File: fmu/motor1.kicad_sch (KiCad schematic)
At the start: 12 parts, among them J4 2213932-3, U4 MCF8316A1VRGFR

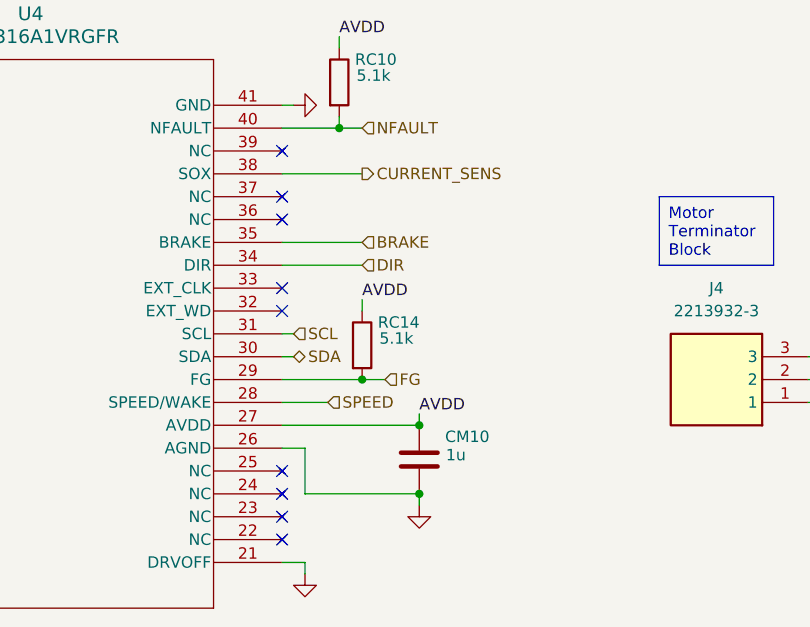
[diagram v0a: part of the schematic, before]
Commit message: Connect motors and MCU
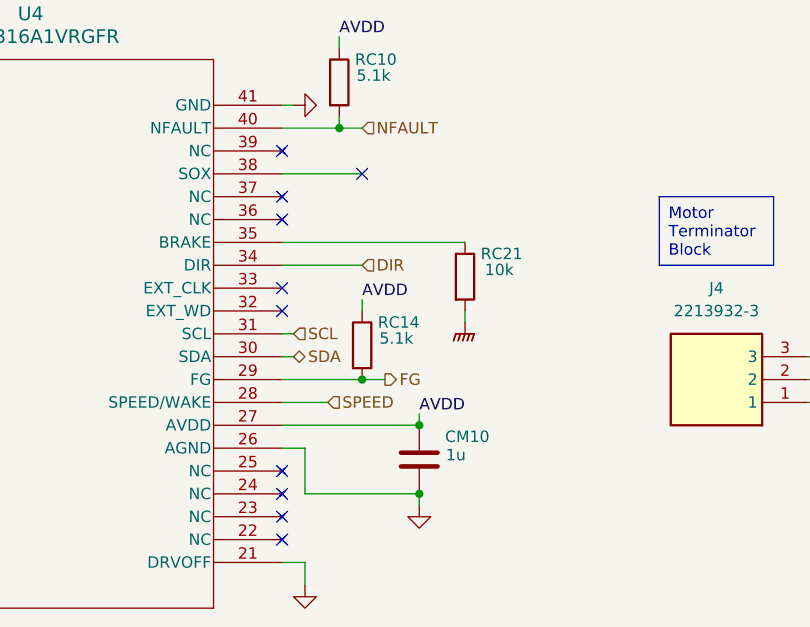
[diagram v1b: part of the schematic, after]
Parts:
- added RC21: 10k, Resistor_SMD:R_0603_1608Metric, symbol Device:R
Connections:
- net GNDPWR: now also RC21.2
- net BRAKE: no longer names the net of U4.35 (BRAKE)
- net BRAKE: now also RC21.1
- net CURRENT_SENS: no longer names the net of U4.38 (SOX)
- no-connect marks 9 -> 10
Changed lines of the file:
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@@
+	)
+	(no_connect
+		(at 156.21 85.09)
 	)
 	(no_connect
@@
 	(wire
 		(pts
-			(xy 149.86 129.54) (xy 149.86 128.27)
-		)
-		(stroke
-			(width 0)
-			(type default)
-		)
-	)
-	(wire
-		(pts
 			(xy 147.32 80.01) (xy 153.67 80.01)
 		)
@@
 	(wire
 		(pts
-			(xy 147.32 92.71) (xy 156.21 92.71)
+			(xy 147.32 92.71) (xy 167.64 92.71)
 		)
 		(stroke
@@
 	(wire
 		(pts
+			(xy 149.86 128.27) (xy 149.86 130.81)
+		)
+		(stroke
+			(width 0)
+			(type default)
+		)
+	)
+	(wire
+		(pts
 			(xy 91.44 115.57) (xy 91.44 118.11)
 		)
@@
 		(pts
 			(xy 147.32 85.09) (xy 156.21 85.09)
+		)
+		(stroke
+			(width 0)
+			(type default)
+		)
+	)
+	(wire
+		(pts
+			(xy 167.64 100.33) (xy 167.64 101.6)
 		)
 		(stroke
@@
 			)
 			(justify left bottom)
-		)
-	)
-	(hierarchical_label "CURRENT_SENS"
-		(shape output)
-		(at 156.21 85.09 0)
-		(fields_autoplaced yes)
-		(effects
-			(font
-				(size 1.27 1.27)
-			)
-			(justify left)
 		)
 	)
@@
 		)
 	)
-	(hierarchical_label "BRAKE"
-		(shape input)
-		(at 156.21 92.71 0)
-		(fields_autoplaced yes)
-		(effects
-			(font
-				(size 1.27 1.27)
-			)
-			(justify left)
-		)
-	)
 	(hierarchical_label "NFAULT"
 		(shape input)
@@
 	)
 	(hierarchical_label "FG"
-		(shape input)
+		(shape output)
 		(at 158.75 107.95 0)
 		(fields_autoplaced yes)
@@
 	)
 	(symbol
-		(lib_id "power:GND")
-		(at 149.86 129.54 0)
-		(unit 1)
-		(exclude_from_sim no)
-		(in_bom yes)
-		(on_board yes)
-		(dnp no)
-		(fields_autoplaced yes)
-		(property "Reference" "#PWR097"
-			(at 149.86 135.89 0)
-			(effects
-				(font
-					(size 1.27 1.27)
-				)
-				(hide yes)
-			)
-		)
-		(property "Value" "GND"
-			(at 149.86 134.62 0)
-			(effects
-				(font
-					(size 1.27 1.27)
-				)
-				(hide yes)
-			)
-		)
-		(property "Footprint" ""
-			(at 149.86 129.54 0)
-			(effects
-				(font
-					(size 1.27 1.27)
-				)
-				(hide yes)
-			)
-		)
-		(property "Datasheet" ""
-			(at 149.86 129.54 0)
-			(effects
-				(font
-					(size 1.27 1.27)
-				)
-				(hide yes)
-			)
-		)
-		(property "Description" "Power symbol creates a global label with name \"GND\" , ground"
-			(at 149.86 129.54 0)
-			(effects
-				(font
-					(size 1.27 1.27)
-				)
-				(hide yes)
-			)
-		)
-		(pin "1"
-		)
-		(instances
-			(project "fmu"
-				(path "/4752d952-9322-46fb-9cc2-2404eb91f5a4/0ffba389-7767-4897-a9a6-36168be44beb"
-					(reference "#PWR097")
-					(unit 1)
-				)
-				(path "/4752d952-9322-46fb-9cc2-2404eb91f5a4/b967478c-5af9-47cc-ac54-cb6f38bbb168"
-					(reference "#PWR098")
-					(unit 1)
-				)
-				(path "/4752d952-9322-46fb-9cc2-2404eb91f5a4/5b8a454b-98f0-4fa4-a9e7-894b0c3f9d86"
-					(reference "#PWR099")
-					(unit 1)
-				)
-				(path "/4752d952-9322-46fb-9cc2-2404eb91f5a4/46b5d8da-e763-4f93-9e8f-7132b5d9fd7e"
-					(reference "#PWR0100")
-					(unit 1)
-				)
-			)
-		)
-	)
-	(symbol
 		(lib_id "Device:C")
 		(at 71.12 105.41 180)
@@
 				(path "/4752d952-9322-46fb-9cc2-2404eb91f5a4/46b5d8da-e763-4f93-9e8f-7132b5d9fd7e"
 					(reference "#PWR078")
+					(unit 1)
+				)
+			)
+		)
+	)
+	(symbol
+		(lib_id "power:GND")
+		(at 149.86 130.81 0)
+		(unit 1)
+		(exclude_from_sim no)
+		(in_bom yes)
+		(on_board yes)
+		(dnp no)
+		(fields_autoplaced yes)
+		(property "Reference" "#PWR097"
+			(at 149.86 137.16 0)
+			(effects
+				(font
+					(size 1.27 1.27)
+				)
+				(hide yes)
+			)
+		)
+		(property "Value" "GND"
+			(at 149.86 135.89 0)
+			(effects
+				(font
+					(size 1.27 1.27)
+				)
+				(hide yes)
+			)
+		)
+		(property "Footprint" ""
+			(at 149.86 130.81 0)
+			(effects
+				(font
+					(size 1.27 1.27)
+				)
+				(hide yes)
+			)
+		)
+		(property "Datasheet" ""
+			(at 149.86 130.81 0)
+			(effects
+				(font
+					(size 1.27 1.27)
+				)
+				(hide yes)
+			)
+		)
+		(property "Description" "Power symbol creates a global label with name \"GND\" , ground"
+			(at 149.86 130.81 0)
+			(effects
+				(font
+					(size 1.27 1.27)
+				)
+				(hide yes)
+			)
+		)
+		(pin "1"
+		)
+		(instances
+			(project "fmu"
+				(path "/4752d952-9322-46fb-9cc2-2404eb91f5a4/0ffba389-7767-4897-a9a6-36168be44beb"
+					(reference "#PWR097")
+					(unit 1)
+				)
+				(path "/4752d952-9322-46fb-9cc2-2404eb91f5a4/b967478c-5af9-47cc-ac54-cb6f38bbb168"
+					(reference "#PWR098")
+					(unit 1)
+				)
+				(path "/4752d952-9322-46fb-9cc2-2404eb91f5a4/5b8a454b-98f0-4fa4-a9e7-894b0c3f9d86"
+					(reference "#PWR099")
+					(unit 1)
+				)
+				(path "/4752d952-9322-46fb-9cc2-2404eb91f5a4/46b5d8da-e763-4f93-9e8f-7132b5d9fd7e"
+					(reference "#PWR0100")
+					(unit 1)
+				)
+			)
+		)
+	)
+	(symbol
+		(lib_id "Device:R")
+		(at 167.64 96.52 0)
+		(unit 1)
+		(exclude_from_sim no)
+		(in_bom yes)
+		(on_board yes)
+		(dnp no)
+		(property "Reference" "RC21"
+			(at 171.704 93.98 0)
+			(effects
+				(font
+					(size 1.27 1.27)
+				)
+			)
+		)
+		(property "Value" "10k"
+			(at 171.45 95.758 0)
+			(effects
+				(font
+					(size 1.27 1.27)
+				)
+			)
+		)
+		(property "Footprint" "Resistor_SMD:R_0603_1608Metric"
+			(at 165.862 96.52 90)
+			(effects
+				(font
+					(size 1.27 1.27)
+				)
+				(hide yes)
+			)
+		)
+		(property "Datasheet" "~"
+			(at 167.64 96.52 0)
+			(effects
+				(font
+					(size 1.27 1.27)
+				)
+				(hide yes)
+			)
+		)
+		(property "Description" "Resistor"
+			(at 167.64 96.52 0)
+			(effects
+				(font
+					(size 1.27 1.27)
+				)
+				(hide yes)
+			)
+		)
+		(property "Power" ""
+			(at 167.64 96.52 90)
+			(effects
+				(font
+					(size 1.27 1.27)
+				)
+				(hide yes)
+			)
+		)
+		(property "Max. Vol" ""
+			(at 167.64 96.52 90)
+			(effects
+				(font
+					(size 1.27 1.27)
+				)
+				(hide yes)
+			)
+		)
+		(pin "2"
+		)
+		(pin "1"
+		)
+		(instances
+			(project "fmu"
+				(path "/4752d952-9322-46fb-9cc2-2404eb91f5a4/0ffba389-7767-4897-a9a6-36168be44beb"
+					(reference "RC21")
+					(unit 1)
+				)
+				(path "/4752d952-9322-46fb-9cc2-2404eb91f5a4/b967478c-5af9-47cc-ac54-cb6f38bbb168"
+					(reference "RC22")
+					(unit 1)
+				)
+				(path "/4752d952-9322-46fb-9cc2-2404eb91f5a4/5b8a454b-98f0-4fa4-a9e7-894b0c3f9d86"
+					(reference "RC23")
+					(unit 1)
+				)
+				(path "/4752d952-9322-46fb-9cc2-2404eb91f5a4/46b5d8da-e763-4f93-9e8f-7132b5d9fd7e"
+					(reference "RC24")
 					(unit 1)
 				)
@@
 					(unit 1)
 				)
+			)
+		)
+	)
+	(symbol
+		(lib_id "power:GNDPWR")
+		(at 167.64 101.6 0)
+		(unit 1)
+		(exclude_from_sim no)
+		(in_bom yes)
+		(on_board yes)
+		(dnp no)
+		(property "Reference" "#PWR016"
+			(at 167.64 106.68 0)
+			(effects
+				(font
+					(size 1.27 1.27)
+				)
+				(hide yes)
+			)
+		)
+		(property "Value" "GNDPWR"
+			(at 162.052 101.854 0)
+			(effects
+				(font
+					(size 1.27 1.27)
+				)
+				(hide yes)
+			)
+		)
+		(property "Footprint" ""
+			(at 167.64 102.87 0)
+			(effects
+				(font
+					(size 1.27 1.27)
+				)
+				(hide yes)
+			)
+		)
+		(property "Datasheet" ""
+			(at 167.64 102.87 0)
+			(effects
+				(font
+					(size 1.27 1.27)
+				)
+				(hide yes)
+			)
+		)
+		(property "Description" "Power symbol creates a global label with name \"GNDPWR\" , global ground"
+			(at 167.64 101.6 0)
+			(effects
+				(font
+					(size 1.27 1.27)
+				)
+				(hide yes)
+			)
+		)
+		(pin "1"
+		)
+		(instances
+			(project "fmu"
+				(path "/4752d952-9322-46fb-9cc2-2404eb91f5a4/0ffba389-7767-4897-a9a6-36168be44beb"
+					(reference "#PWR016")
+					(unit 1)
+				)
+				(path "/4752d952-9322-46fb-9cc2-2404eb91f5a4/b967478c-5af9-47cc-ac54-cb6f38bbb168"
+					(reference "#PWR017")
+					(unit 1)
+				)
+				(path "/4752d952-9322-46fb-9cc2-2404eb91f5a4/5b8a454b-98f0-4fa4-a9e7-894b0c3f9d86"
+					(reference "#PWR091")
+					(unit 1)
+				)
+				(path "/4752d952-9322-46fb-9cc2-2404eb91f5a4/46b5d8da-e763-4f93-9e8f-7132b5d9fd7e"
+					(reference "#PWR093")
+					(unit 1)
+				)
